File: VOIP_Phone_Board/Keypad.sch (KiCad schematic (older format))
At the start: 0 parts

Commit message: Add keypad.
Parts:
- added J2: KeypadConnector, Connector_PinHeader_2.54mm:PinHeader_1x08_P2.54mm_Vertical, symbol Keypad:KeypadConnector
- added KM1: KeypadMount, VOIP_Phone_Board:Keypad_mounting, symbol Keypad:KeypadMount
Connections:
- new net Column1: J2.4 (Column_1)
- new net Column2: J2.3 (Column_2)
- new net Column3: J2.2 (Column_3)
- new net Column4: J2.1 (Column_4)
- new net Row1: J2.8 (Row_1)
- new net Row2: J2.7 (Row_2)
- new net Row3: J2.6 (Row_3)
- new net Row4: J2.5 (Row_4)
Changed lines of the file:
@@
 $Descr A4 11693 8268
 encoding utf-8
-Sheet 1 4
+Sheet 3 4
 Title ""
 Date ""
@@
 Comment4 ""
 $EndDescr
+$Comp
+L Keypad:KeypadMount KM1
+U 1 1 625DCF80
+P 7100 3000
+F 0 "KM1" H 7378 3046 50  0000 L CNN
+F 1 "KeypadMount" H 7378 2955 50  0000 L CNN
+F 2 "VOIP_Phone_Board:Keypad_mounting" H 7100 3000 50  0001 C CNN
+F 3 "" H 7100 3000 50  0001 C CNN
+	1    7100 3000
+	1    0    0    -1
+$EndComp
+Text HLabel 5350 2650 0    50   Input ~ 0
+Column4
+Text HLabel 5350 2750 0    50   Input ~ 0
+Column3
+Text HLabel 5350 2850 0    50   Input ~ 0
+Column2
+Text HLabel 5350 2950 0    50   Input ~ 0
+Column1
+Text HLabel 5350 3050 0    50   Output ~ 0
+Row4
+Text HLabel 5350 3150 0    50   Output ~ 0
+Row3
+Text HLabel 5350 3250 0    50   Output ~ 0
+Row2
+Text HLabel 5350 3350 0    50   Output ~ 0
+Row1
+Wire Wire Line
+	5500 2650 5350 2650
+Wire Wire Line
+	5500 2750 5350 2750
+Wire Wire Line
+	5500 2850 5350 2850
+Wire Wire Line
+	5500 2950 5350 2950
+Wire Wire Line
+	5500 3050 5350 3050
+Wire Wire Line
+	5500 3150 5350 3150
+Wire Wire Line
+	5500 3250 5350 3250
+Wire Wire Line
+	5500 3350 5350 3350
+$Comp
+L Keypad:KeypadConnector J2
+U 1 1 625E8DC1
+P 5700 2950
+F 0 "J2" H 5672 2924 50  0000 R CNN
+F 1 "KeypadConnector" H 5672 2833 50  0000 R CNN
+F 2 "Connector_PinHeader_2.54mm:PinHeader_1x08_P2.54mm_Vertical" H 5700 2950 50  0001 C CNN
+F 3 "~" H 5700 2950 50  0001 C CNN
+	1    5700 2950
+	-1   0    0    -1
+$EndComp
 $EndSCHEMATC

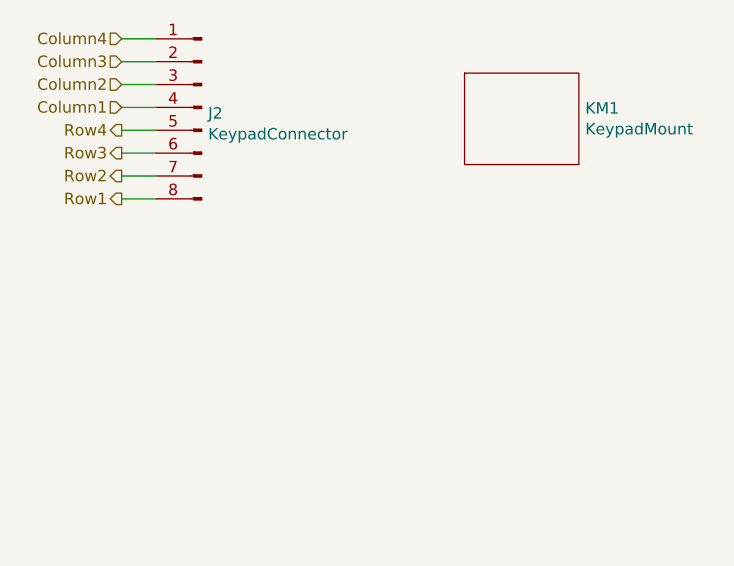
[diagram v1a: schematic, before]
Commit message: Add Hook Switch.
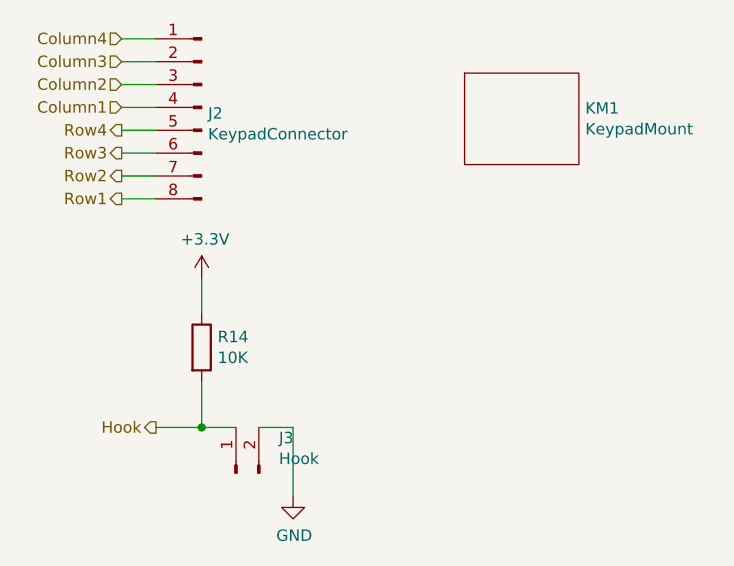
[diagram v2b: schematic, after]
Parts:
- added J3: Hook, Connector_PinHeader_2.54mm:PinHeader_1x02_P2.54mm_Vertical, symbol Connector:Conn_01x02_Male
- added R14: 10K, Resistor_SMD:R_0603_1608Metric_Pad1.05x0.95mm_HandSolder, symbol Device:R
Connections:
- new net +3V3: R14.1
- new net GND: J3.2 (Pin_2)
- new net Hook: J3.1 (Pin_1), R14.2
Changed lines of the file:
@@
 	-1   0    0    -1
 $EndComp
+$Comp
+L power:GND #PWR024
+U 1 1 625ED319
+P 6100 4650
+F 0 "#PWR024" H 6100 4400 50  0001 C CNN
+F 1 "GND" H 6105 4477 50  0000 C CNN
+F 2 "" H 6100 4650 50  0001 C CNN
+F 3 "" H 6100 4650 50  0001 C CNN
+	1    6100 4650
+	1    0    0    -1
+$EndComp
+$Comp
+L Device:R R14
+U 1 1 625ED464
+P 5700 4000
+F 0 "R14" H 5770 4046 50  0000 L CNN
+F 1 "10K" H 5770 3955 50  0000 L CNN
+F 2 "Resistor_SMD:R_0603_1608Metric_Pad1.05x0.95mm_HandSolder" V 5630 4000 50  0001 C CNN
+F 3 "~" H 5700 4000 50  0001 C CNN
+F 4 "603-AC0603DR-0710KL" H 5700 4000 50  0001 C CNN "Mouser Part Number"
+	1    5700 4000
+	1    0    0    -1
+$EndComp
+$Comp
+L power:+3.3V #PWR023
+U 1 1 625ED807
+P 5700 3700
+F 0 "#PWR023" H 5700 3550 50  0001 C CNN
+F 1 "+3.3V" H 5715 3873 50  0000 C CNN
+F 2 "" H 5700 3700 50  0001 C CNN
+F 3 "" H 5700 3700 50  0001 C CNN
+	1    5700 3700
+	1    0    0    -1
+$EndComp
+Wire Wire Line
+	5700 3700 5700 3850
+Wire Wire Line
+	5700 4150 5700 4350
+Wire Wire Line
+	6100 4350 6100 4650
+Text HLabel 5500 4350 0    50   Output ~ 0
+Hook
+Wire Wire Line
+	5500 4350 5700 4350
+$Comp
+L Connector:Conn_01x02_Male J3
+U 1 1 625EFA0E
+P 5850 4550
+F 0 "J3" V 6004 4362 50  0000 R CNN
+F 1 "Hook" V 5913 4362 50  0000 R CNN
+F 2 "Connector_PinHeader_2.54mm:PinHeader_1x02_P2.54mm_Vertical" H 5850 4550 50  0001 C CNN
+F 3 "~" H 5850 4550 50  0001 C CNN
+	1    5850 4550
+	0    -1   -1   0
+$EndComp
+Wire Wire Line
+	5950 4350 6100 4350
+Wire Wire Line
+	5850 4350 5700 4350
+Connection ~ 5700 4350
 $EndSCHEMATC
